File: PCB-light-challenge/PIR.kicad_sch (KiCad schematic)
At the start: 1 part

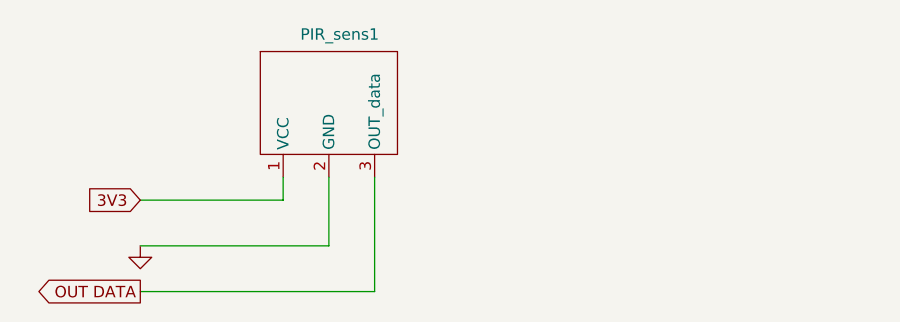
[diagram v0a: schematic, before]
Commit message: Mainboard onderdelen gesorteerd
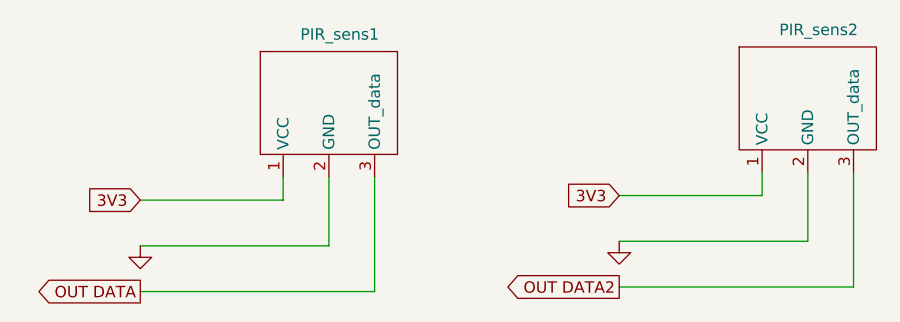
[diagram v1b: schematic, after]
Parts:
- added PIR_sens2: ~, PIRsens:PIR-SENS, symbol PIRsens:PIR
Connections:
- net 3V3: now also PIR_sens2.1 (VCC)
- net GND: now also PIR_sens2.2 (GND)
- new net OUT DATA2: PIR_sens2.3 (OUT_data)
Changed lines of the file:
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@@
     (company "HHS Living Labs")
   )
+  (wire (pts (xy 161.163 56.642) (xy 161.163 69.342))
+    (stroke (width 0) (type default))
+  )
   (wire (pts (xy 102.87 57.15) (xy 102.87 64.77))
+    (stroke (width 0) (type default))
+  )
+  (wire (pts (xy 135.128 69.342) (xy 161.163 69.342))
+    (stroke (width 0) (type default))
+  )
+  (wire (pts (xy 135.128 59.182) (xy 151.003 59.182))
     (stroke (width 0) (type default))
   )
@@
   )
   (wire (pts (xy 81.915 64.77) (xy 102.87 64.77))
+    (stroke (width 0) (type default))
+  )
+  (wire (pts (xy 135.128 64.262) (xy 156.083 64.262))
+    (stroke (width 0) (type default))
+  )
+  (wire (pts (xy 151.003 56.642) (xy 151.003 59.182))
+    (stroke (width 0) (type default))
+  )
+  (wire (pts (xy 156.083 56.642) (xy 156.083 64.262))
     (stroke (width 0) (type default))
   )
@@
     (property "Intersheetrefs" "${INTERSHEET_REFS}" (at 75.5016 59.69 0)
       (effects (font (size 1.27 1.27)) (justify right) hide)
+    )
+  )
+  (global_label "OUT DATA2" (shape output) (at 135.128 69.342 180) (fields_autoplaced)
+    (effects (font (size 1.27 1.27)) (justify right))
+    (property "Intersheetrefs" "${INTERSHEET_REFS}" (at 122.2073 69.342 0)
+      (effects (font (size 1.27 1.27)) (justify right) hide)
+    )
+  )
+  (global_label "3V3" (shape input) (at 135.128 59.182 180) (fields_autoplaced)
+    (effects (font (size 1.27 1.27)) (justify right))
+    (property "Intersheetrefs" "${INTERSHEET_REFS}" (at 128.7146 59.182 0)
+      (effects (font (size 1.27 1.27)) (justify right) hide)
+    )
+  )
+  (symbol (lib_id "PIRsens:PIR") (at 156.083 45.212 0) (unit 1)
+    (in_bom yes) (on_board yes) (dnp no)
+    (property "Reference" "PIR_sens2" (at 152.908 40.767 0)
+      (effects (font (size 1.27 1.27)) (justify left))
+    )
+    (property "Value" "~" (at 156.083 45.212 0)
+      (effects (font (size 1.27 1.27)))
+    )
+    (property "Footprint" "PIRsens:PIR-SENS" (at 156.083 45.212 0)
+      (effects (font (size 1.27 1.27)) hide)
+    )
+    (property "Datasheet" "" (at 156.083 45.212 0)
+      (effects (font (size 1.27 1.27)) hide)
+    )
+    (pin "1")
+    (pin "2")
+    (pin "3")
+    (instances
+      (project "PCB-light-challenge"
+        (path "/35573e8f-7834-430c-81d2-239f316c7834/5679ea21-1e58-482d-afee-07308fc996bf"
+          (reference "PIR_sens2") (unit 1)
+        )
+      )
     )
   )
@@
         )
       )
+    )
+  )
+  (symbol (lib_id "power:GND") (at 135.128 64.262 0) (unit 1)
+    (in_bom yes) (on_board yes) (dnp no) (fields_autoplaced)
+    (property "Reference" "#PWR03" (at 135.128 70.612 0)
+      (effects (font (size 1.27 1.27)) hide)
+    )
+    (property "Value" "GND" (at 135.128 68.3975 0)
+      (effects (font (size 1.27 1.27)) hide)
+    )
+    (property "Footprint" "" (at 135.128 64.262 0)
+      (effects (font (size 1.27 1.27)) hide)
+    )
+    (property "Datasheet" "" (at 135.128 64.262 0)
+      (effects (font (size 1.27 1.27)) hide)
+    )
+    (pin "1")
+    (instances
+      (project "PCB-light-challenge"
+        (path "/35573e8f-7834-430c-81d2-239f316c7834/5679ea21-1e58-482d-afee-07308fc996bf"
+          (reference "#PWR03") (unit 1)
+        )
+      )

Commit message: main board aangepast en ground toegevoegd
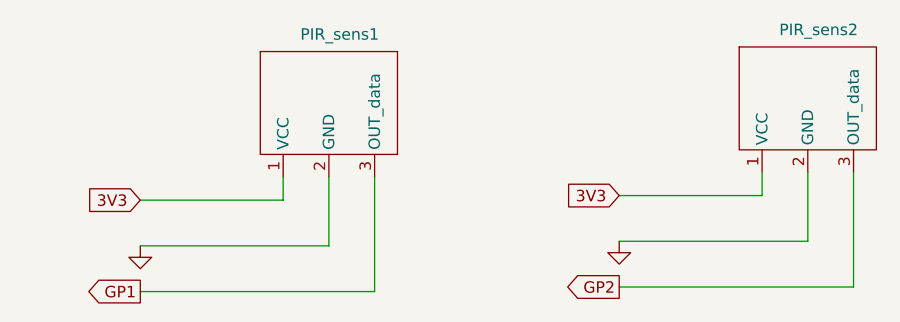
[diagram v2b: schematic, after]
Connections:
- net OUT DATA renamed GP1
- net OUT DATA2 renamed GP2
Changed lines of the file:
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@@
     (stroke (width 0) (type default))
   )
-  (global_label "OUT DATA" (shape output) (at 81.915 69.85 180) (fields_autoplaced)
+  (global_label "GP1" (shape output) (at 81.915 69.85 180) (fields_autoplaced)
     (effects (font (size 1.27 1.27)) (justify right))
-    (property "Intersheetrefs" "${INTERSHEET_REFS}" (at 70.2038 69.85 0)
+    (property "Intersheetrefs" "${INTERSHEET_REFS}" (at 75.2597 69.85 0)
       (effects (font (size 1.27 1.27)) (justify right) hide)
     )
@@
     )
   )
-  (global_label "OUT DATA2" (shape output) (at 135.128 69.342 180) (fields_autoplaced)
+  (global_label "GP2" (shape output) (at 135.128 69.342 180) (fields_autoplaced)
     (effects (font (size 1.27 1.27)) (justify right))
-    (property "Intersheetrefs" "${INTERSHEET_REFS}" (at 122.2073 69.342 0)
+    (property "Intersheetrefs" "${INTERSHEET_REFS}" (at 128.4727 69.342 0)
       (effects (font (size 1.27 1.27)) (justify right) hide)
     )

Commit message: PCB 80% af
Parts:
- PIR_sens1, PIR_sens2: footprint PIRsens:PIR-SENS -> Connector_PinHeader_2.54mm:PinHeader_1x03_P2.54mm_Vertical
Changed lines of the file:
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@@
       (effects (font (size 1.27 1.27)))
     )
-    (property "Footprint" "PIRsens:PIR-SENS" (at 156.083 45.212 0)
+    (property "Footprint" "Connector_PinHeader_2.54mm:PinHeader_1x03_P2.54mm_Vertical" (at 156.083 45.212 0)
       (effects (font (size 1.27 1.27)) hide)
     )
@@
       (effects (font (size 1.27 1.27)))
     )
-    (property "Footprint" "PIRsens:PIR-SENS" (at 102.87 45.72 0)
+    (property "Footprint" "Connector_PinHeader_2.54mm:PinHeader_1x03_P2.54mm_Vertical" (at 102.87 45.72 0)
       (effects (font (size 1.27 1.27)) hide)
     )
